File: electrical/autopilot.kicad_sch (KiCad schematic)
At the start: 7 parts

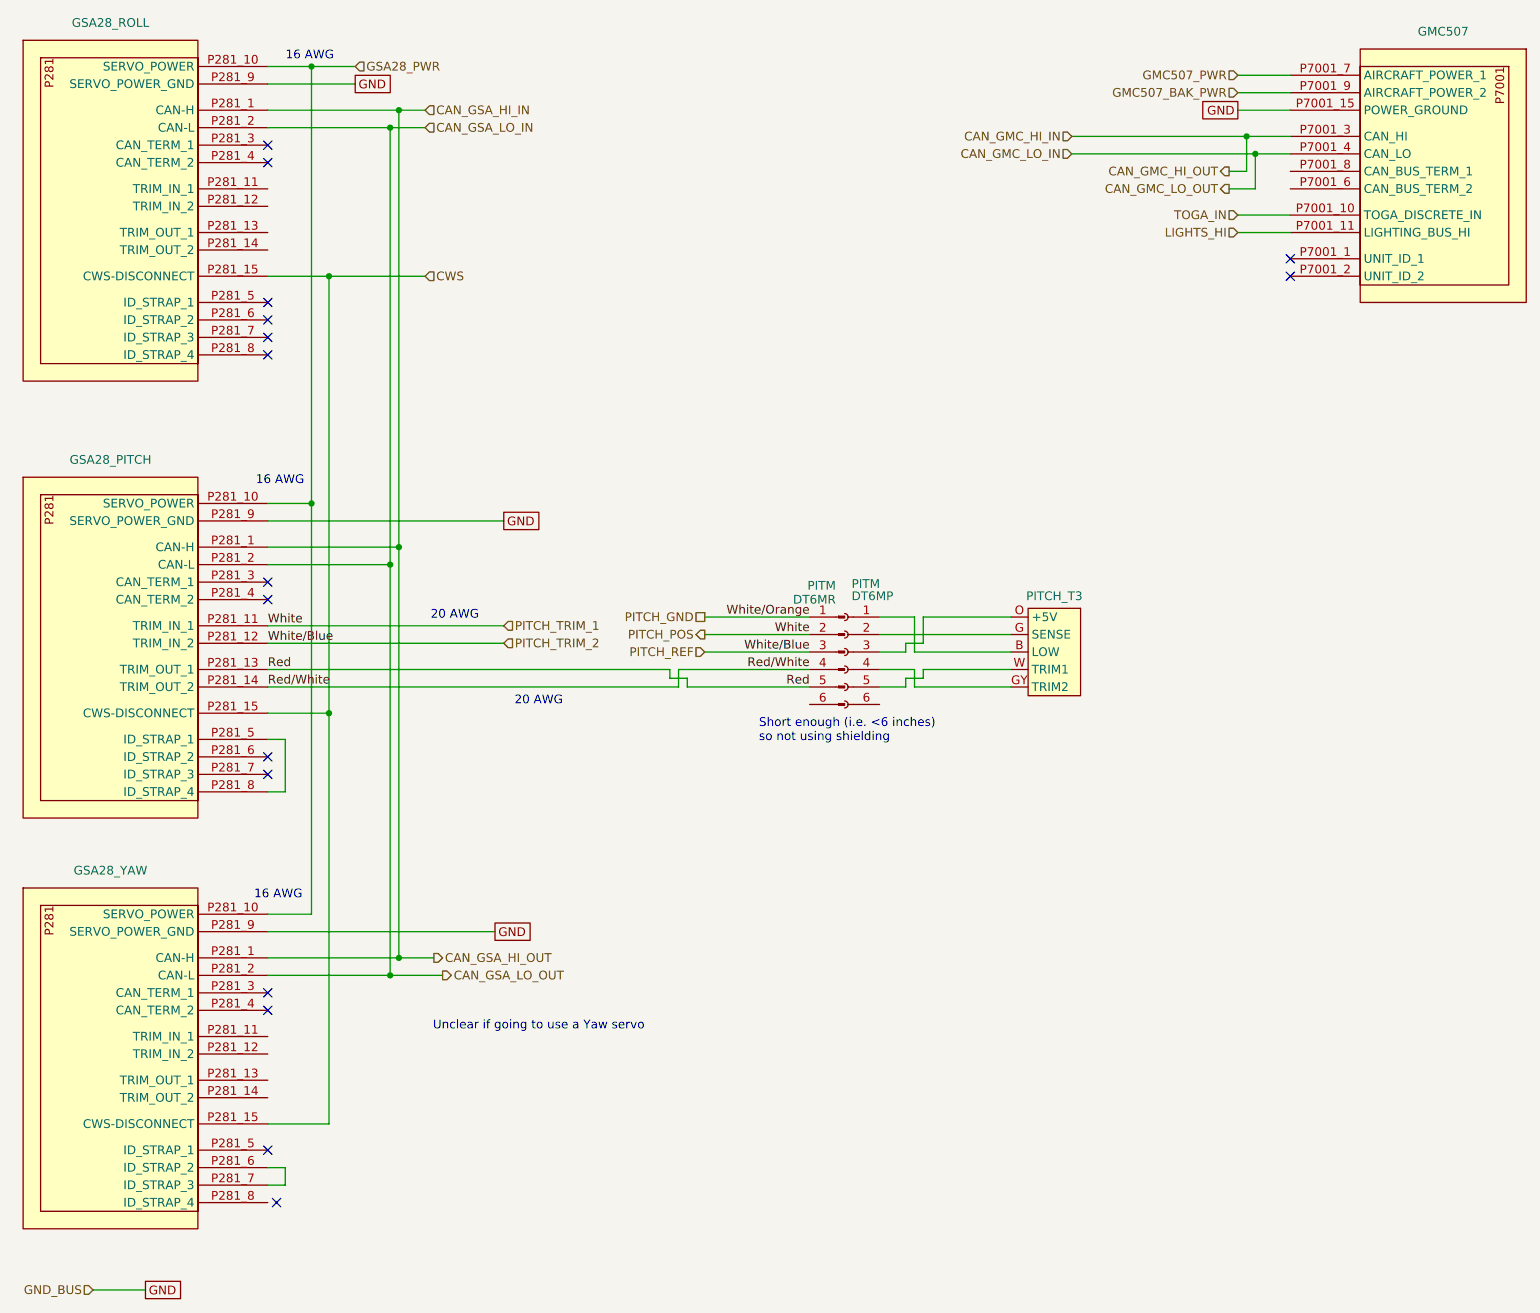
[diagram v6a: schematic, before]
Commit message: Added shielding and wire colors and corrections.
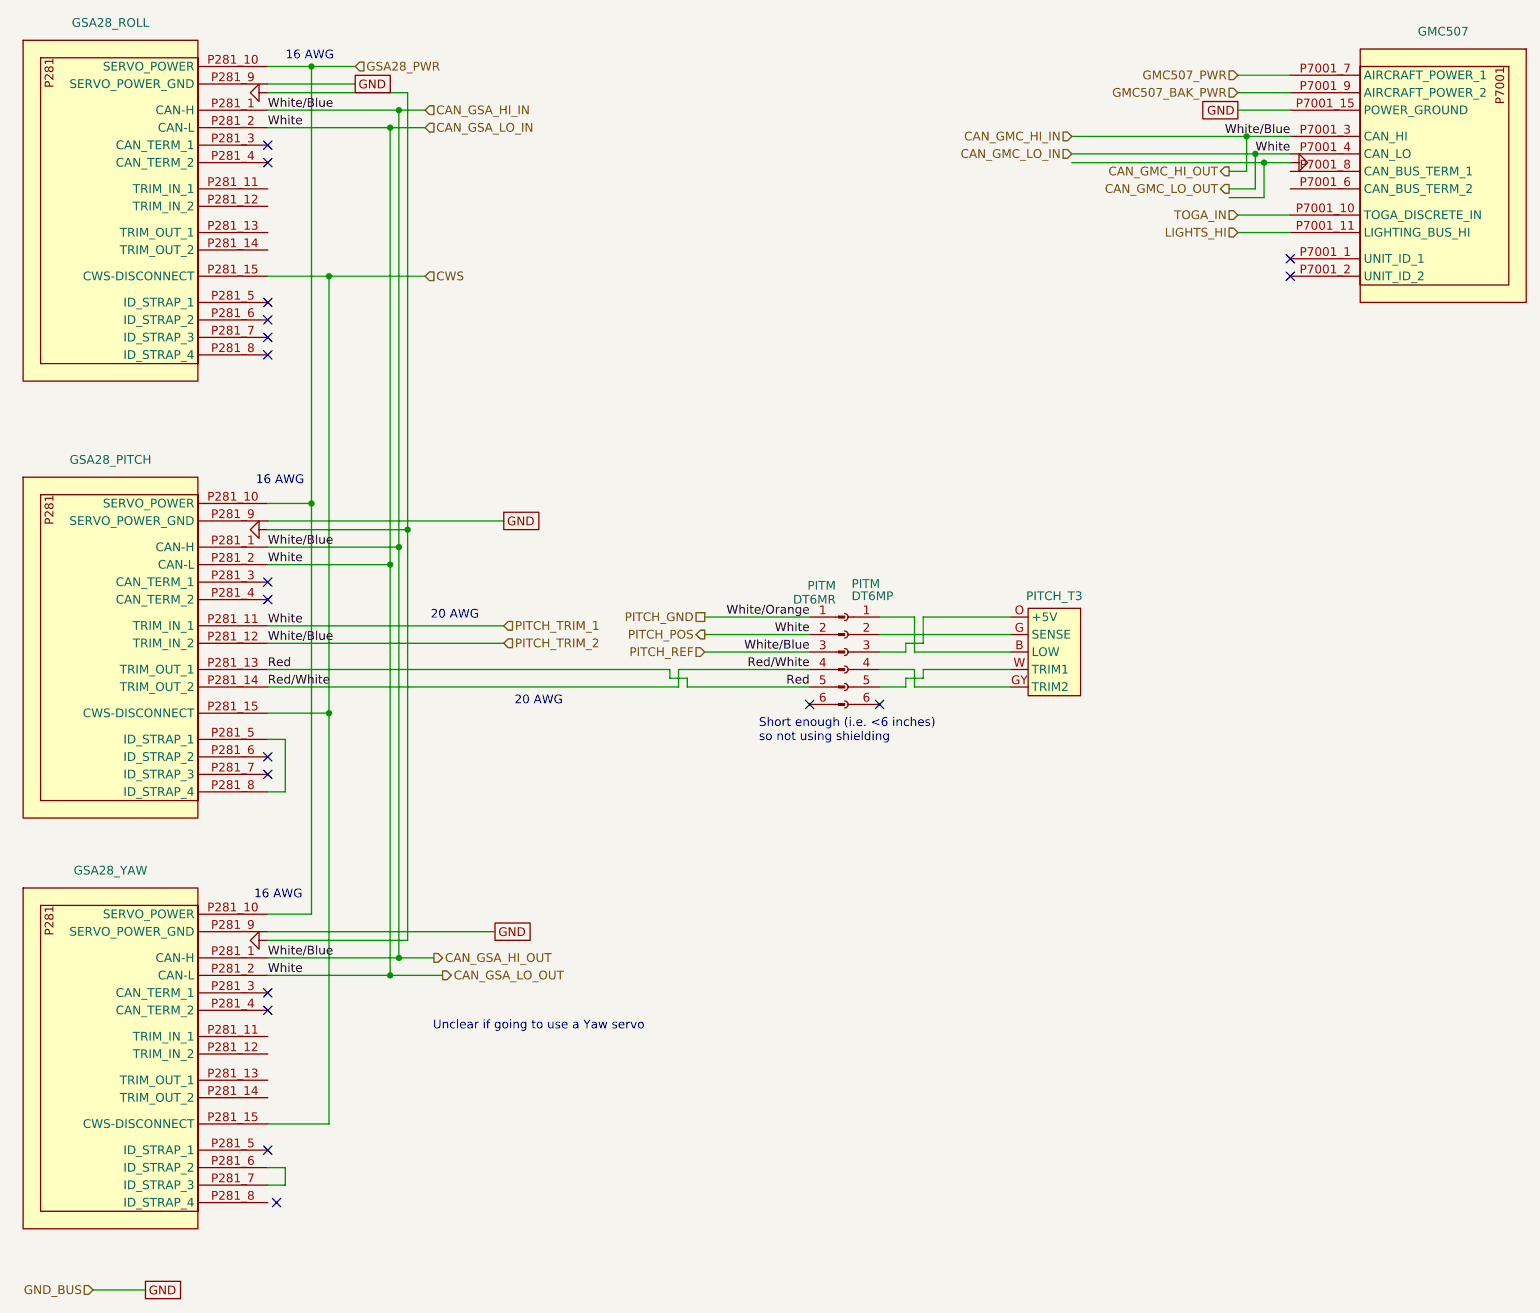
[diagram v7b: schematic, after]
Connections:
- net CAN_GSA_HI_IN is gone; now on net CAN_GMC_HI_IN: GSA28_PITCH.P281_1 (CAN-H), GSA28_ROLL.P281_1 (CAN-H), GSA28_YAW.P281_1 (CAN-H)
- net CAN_GSA_LO_IN is gone; now on net CAN_GMC_LO_IN: GSA28_PITCH.P281_2 (CAN-L), GSA28_ROLL.P281_2 (CAN-L), GSA28_YAW.P281_2 (CAN-L)
- net PITCH_POS is gone; now on net CAN_GMC_LO_IN: GSA28_PITCH.P281_11 (TRIM_IN_1), PITM.2 (Pin_2)
- net PITCH_REF is gone; now on net CAN_GMC_HI_IN: GSA28_PITCH.P281_12 (TRIM_IN_2), PITM.3 (Pin_3)
- no-connect marks 16 -> 18
